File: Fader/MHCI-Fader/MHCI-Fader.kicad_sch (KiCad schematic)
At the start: 1 part

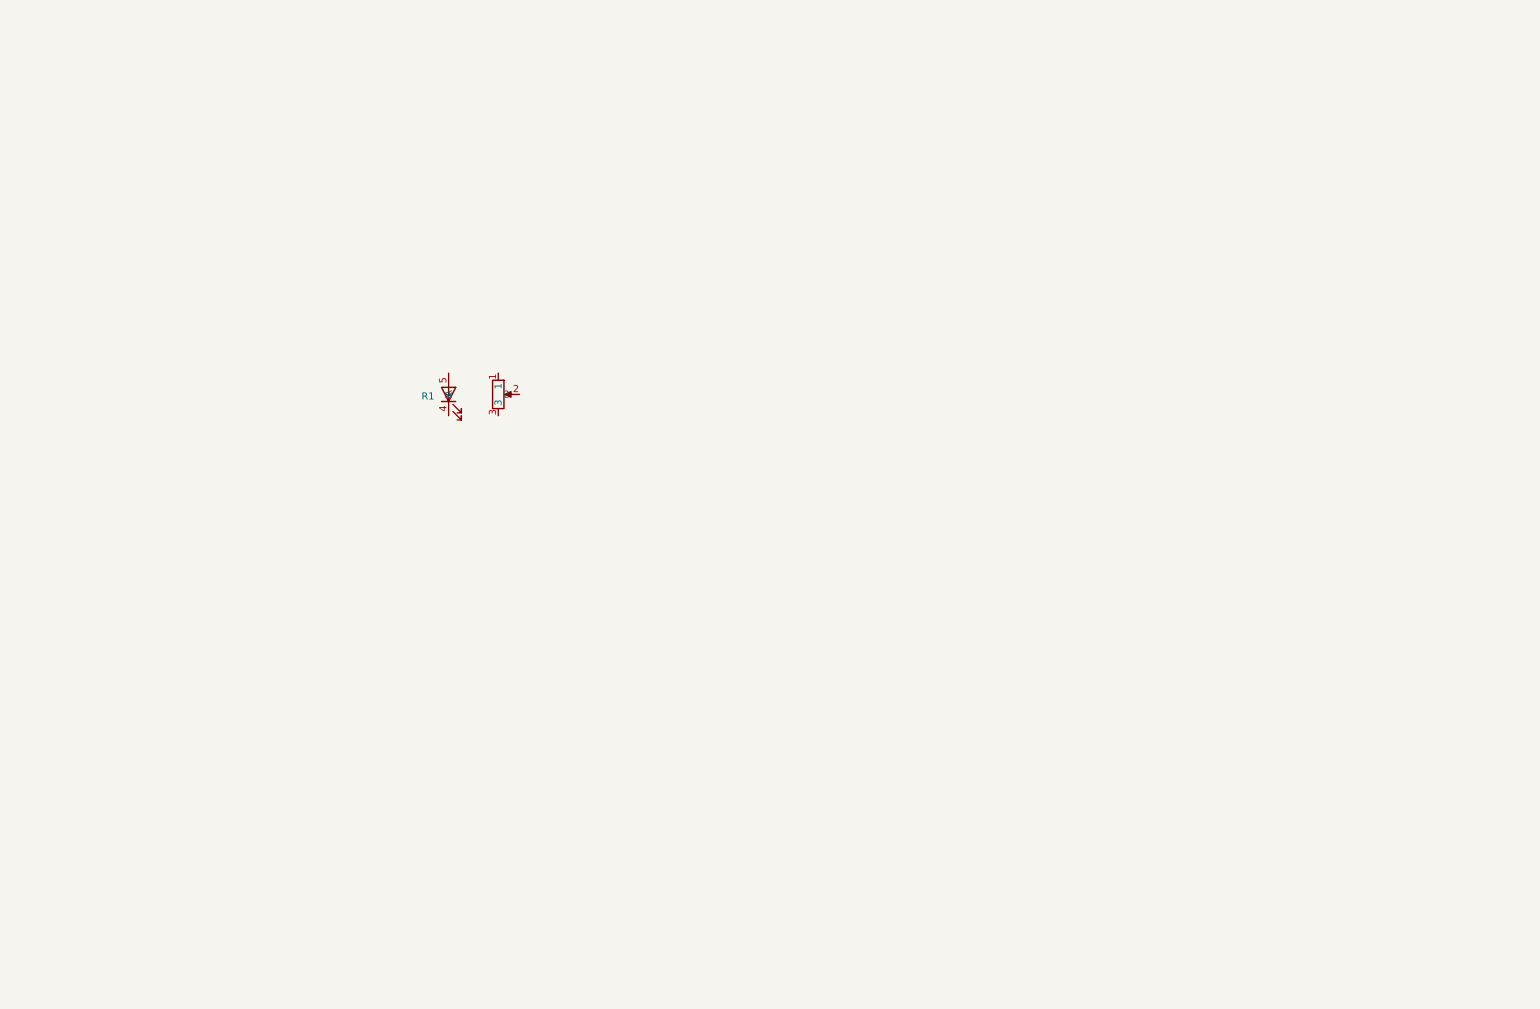
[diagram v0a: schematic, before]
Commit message: Add all Waveshare footprints
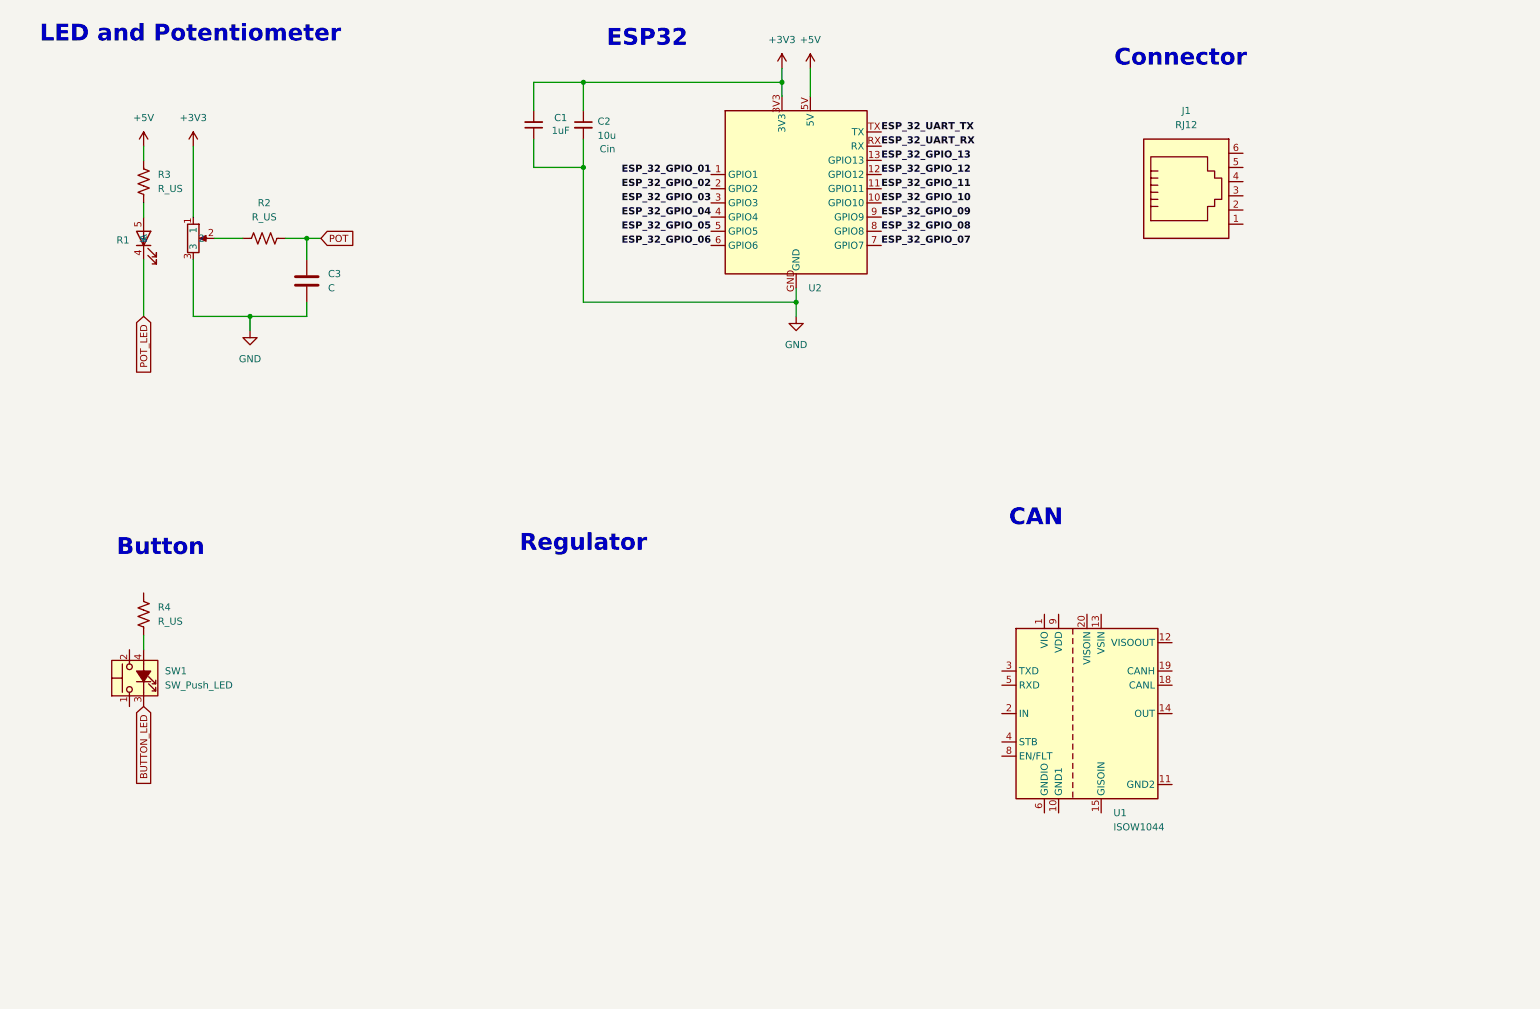
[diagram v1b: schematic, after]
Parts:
- added C1: 1uF, Capacitor_SMD:C_0402_1005Metric, symbol Device:C_Small
- added C2: 10u, Capacitor_SMD:C_0603_1608Metric, symbol Device:C_Small
- added C3: C, symbol Device:C
- added J1: RJ12, Connector_RJ:RJ12_Amphenol_54601-x06_Horizontal, symbol Connector:RJ12
- added R2, R3, R4: R_US, symbol Device:R_US
- added SW1: SW_Push_LED, MCHI:SP86N_AB Switch, symbol Switch:SW_Push_LED
- added U1: ISOW1044, Package_SO:SOIC-20W_7.5x12.8mm_P1.27mm, symbol Interface_CAN_LIN:ISOW1044
- added U2: ~, MCHI:ESP-32-S3-Zero - SMD, symbol MHCI:ESP32-S3-Zero
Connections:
- net +3V3: now reaches R1.1
- net +3V3: now also C1.2, C2.1, U2.3V3
- net at R1.2: now also R2.1
- net GND: now reaches R1.3
- net GND: now also C1.1, C2.2, C3.2, U2.GND
- net POT_LED: now reaches R1.4 (K)
- net at R1.5 (A): now also R3.1
- new net: U1.15 (GISOIN), U1.16 (GISOIN), U1.17 (GISOIN)
- new net: R4.1, SW1.4 (A)
- new net +5V: R3.2, U2.5V
- new net BUTTON_LED: SW1.3 (K)
- new net ESP_32_GPIO_01: U2.1 (GPIO1)
- new net ESP_32_GPIO_02: U2.2 (GPIO2)
- new net ESP_32_GPIO_03: U2.3 (GPIO3)
- new net ESP_32_GPIO_04: U2.4 (GPIO4)
- new net ESP_32_GPIO_05: U2.5 (GPIO5)
- new net ESP_32_GPIO_06: U2.6 (GPIO6)
- new net ESP_32_GPIO_07: U2.7 (GPIO7)
- new net ESP_32_GPIO_08: U2.8 (GPIO8)
- new net ESP_32_GPIO_09: U2.9 (GPIO9)
- new net ESP_32_GPIO_10: U2.10 (GPIO10)
- new net ESP_32_GPIO_11: U2.11 (GPIO11)
- new net ESP_32_GPIO_12: U2.12 (GPIO12)
- new net ESP_32_GPIO_13: U2.13 (GPIO13)
- new net ESP_32_UART_RX: U2.RX
- new net ESP_32_UART_TX: U2.TX
- new net POT: C3.1, R2.2
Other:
- note added: "Button"
- note added: "CAN"
- note added: "Connector"
- note added: "ESP32"
- note added: "LED and Potentiometer"
- note added: "Regulator"
- moved on the sheet: R1

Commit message: Initial fader schematic
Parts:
- removed C3: C, symbol Device:C
- removed J1: RJ12, Connector_RJ:RJ12_Amphenol_54601-x06_Horizontal, symbol Connector:RJ12
- removed U1: ISOW1044, Package_SO:SOIC-20W_7.5x12.8mm_P1.27mm, symbol Interface_CAN_LIN:ISOW1044
- added C3: 10uF, Capacitor_SMD:C_0603_1608Metric, symbol Device:C_Small
- added C4: 1uF, Capacitor_SMD:C_0402_1005Metric, symbol Device:C_Small
- added C5, C7: 100nF, Capacitor_SMD:C_0402_1005Metric, symbol Device:C_Small
- added C6: 1u, Capacitor_SMD:C_0402_1005Metric, symbol Device:C_Small
- added C8: 30pF, Capacitor_SMD:C_0402_1005Metric, symbol Device:C_Small
- added FB1: FerriteBead, Diode_SMD:D_0805_2012Metric, symbol Device:FerriteBead_Small
- added J1: Conn_01x06, Connector_PinHeader_2.54mm:PinHeader_1x06_P2.54mm_Vertical, symbol Connector_Generic:Conn_01x06
- added JP1, JP2: Jumper_2_Open, Jumper:SolderJumper-2_P1.3mm_Open_RoundedPad1.0x1.5mm, symbol Jumper:Jumper_2_Open
- added PS1: TBA1-0510, MCHI:CONV_TBA1-0510, symbol MHCI:TBA1-0510
- added R10, R9: 0R, Resistor_SMD:R_0402_1005Metric, symbol Device:R_US
- added R5, R6: 4K7, Resistor_SMD:R_0603_1608Metric, symbol Device:R_US
- added R7: 10K, Resistor_SMD:R_0402_1005Metric, symbol Device:R_US
- added R8: 120R, Resistor_SMD:R_0402_1005Metric, symbol Device:R_US
- added TP1: VIN, TestPoint:TestPoint_Pad_D1.0mm, symbol Connector:TestPoint
- added TP2: 5V, TestPoint:TestPoint_Pad_D1.0mm, symbol Connector:TestPoint
- added U1: TJA1051T, Package_SO:SOIC-8_3.9x4.9mm_P1.27mm, symbol Interface_CAN_LIN:TJA1051T
- added U3: SRV05-4, Package_TO_SOT_SMD:SOT-23-6, symbol Power_Protection:SRV05-4
- C1: value 1uF -> 100nF; LCSC C52923 -> C1525
- C2: value 10u -> 30pF; footprint Capacitor_SMD:C_0603_1608Metric -> Capacitor_SMD:C_0402_1005Metric; LCSC C19702 -> C1570
- R2, R3, R4: value R_US -> 220R; footprint (none) -> Resistor_SMD:R_0402_1005Metric; LCSC (none) -> C25091
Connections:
- net +3V3: now also R3.2, R4.2, PS1.4 (+VOUT), R5.1, R6.1, R7.1; no longer C1.2, C2.1
- net +5V: now also C1.1, C5.1, FB1.2, JP1.2 (B), PS1.2 (+VIN(VCC)), TP2.1, U1.3 (VCC); no longer R3.2, U2.5V
- net BUTTON_LED: now also C6.1, R7.2
- net GND: now also C1.2, C2.1, SW1.1, C6.2, C7.2, C8.2, PS1.3 (-VOUT), U1.2 (GND); no longer C1.1, C2.2
- net POT: now also R2.1, C7.1; no longer R2.2
- net at R1.2: now also R2.2; no longer R2.1
- new net: JP2.1 (A), R8.2
- new net: JP1.1 (A), U2.5V
- new net CANH: C8.1, J1.4 (Pin_4), R9.1, U3.4 (IO3)
- new net CANH_L: JP2.2 (B), R10.1, U1.6 (CANL)
- new net CANH_T: R8.1, R9.2, U1.7 (CANH)
- new net CANL: C2.2, J1.5 (Pin_5), R10.2, U3.6 (IO4)
- new net CAN_RX: U1.4 (RXD)
- new net CAN_S: U1.8 (S)
- new net CAN_TX: U1.1 (TXD)
- new net Earth: C3.2, C4.1, C5.2, J1.6 (Pin_6), PS1.1 (-VIN(GND)), U3.2 (VN)
- new net SCL: J1.3 (Pin_3), R6.2, U3.3 (IO2)
- new net SDA: J1.2 (Pin_2), R5.2, U3.1 (IO1)
- new net VIN: C3.1, C4.2, FB1.1, J1.1 (Pin_1), TP1.1, U3.5 (VP)
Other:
- note added: "I2C"
- note added: "Power Regulator"
- note added: "Termination"
- note removed: "Regulator"
- moved on the sheet: R1, R3, SW1, U2

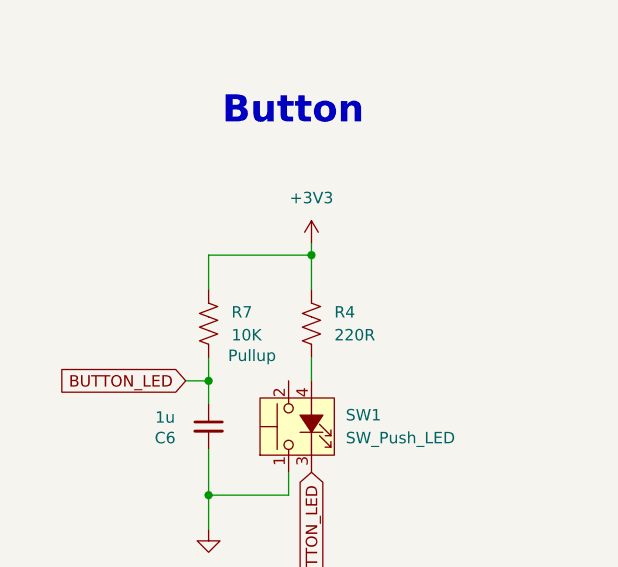
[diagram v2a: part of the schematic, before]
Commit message: Fix button schematic
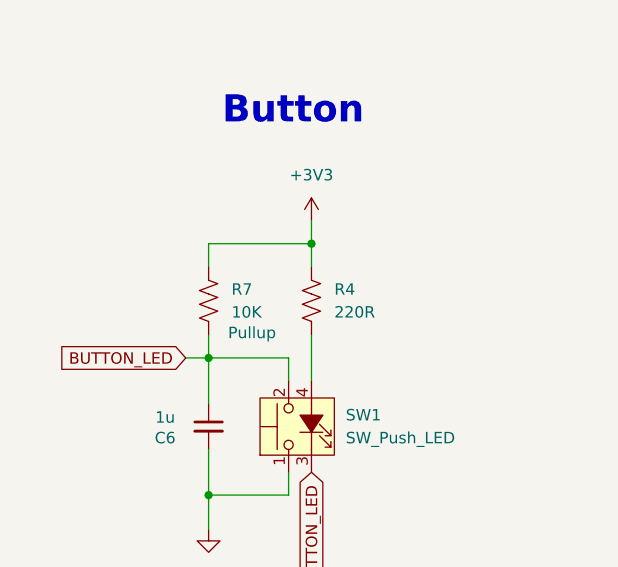
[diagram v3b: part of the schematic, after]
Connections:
- net BUTTON_LED: now also SW1.2
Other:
- moved on the sheet: R4, R7
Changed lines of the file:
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@@
 	(paper "A4")
 	(junction
-		(at 36.83 116.84)
-		(diameter 0)
-		(color 0 0 0 0)
-	)
-	(junction
 		(at 53.34 170.18)
 		(diameter 0)
@@
 	)
 	(junction
-		(at 68.58 170.18)
+		(at 48.26 101.6)
 		(diameter 0)
 		(color 0 0 0 0)
 	)
 	(junction
-		(at 222.25 102.87)
+		(at 68.58 170.18)
 		(diameter 0)
 		(color 0 0 0 0)
 	)
 	(junction
-		(at 48.26 102.87)
+		(at 222.25 102.87)
 		(diameter 0)
 		(color 0 0 0 0)
@@
 	)
 	(junction
+		(at 36.83 114.3)
+		(diameter 0)
+		(color 0 0 0 0)
+	)
+	(junction
 		(at 53.34 181.61)
 		(diameter 0)
@@
 	(wire
 		(pts
-			(xy 262.89 130.81) (xy 262.89 133.35)
+			(xy 45.72 114.3) (xy 45.72 116.84)
 		)
 		(stroke
@@
 	(wire
 		(pts
-			(xy 36.83 116.84) (xy 36.83 119.38)
+			(xy 262.89 130.81) (xy 262.89 133.35)
 		)
 		(stroke
@@
 	(wire
 		(pts
-			(xy 48.26 102.87) (xy 48.26 106.68)
-		)
-		(stroke
-			(width 0)
-			(type default)
-		)
-	)
-	(wire
-		(pts
 			(xy 252.73 130.81) (xy 252.73 128.27)
 		)
@@
 	(wire
 		(pts
-			(xy 36.83 114.3) (xy 36.83 116.84)
-		)
-		(stroke
-			(width 0)
-			(type default)
-		)
-	)
-	(wire
-		(pts
 			(xy 43.18 63.5) (xy 53.34 63.5)
 		)
@@
 	(wire
 		(pts
-			(xy 34.29 116.84) (xy 36.83 116.84)
+			(xy 34.29 114.3) (xy 36.83 114.3)
 		)
 		(stroke
@@
 	(wire
 		(pts
-			(xy 48.26 102.87) (xy 48.26 101.6)
-		)
-		(stroke
-			(width 0)
-			(type default)
-		)
-	)
-	(wire
-		(pts
 			(xy 43.18 33.02) (xy 43.18 45.72)
 		)
@@
 	(wire
 		(pts
+			(xy 48.26 99.06) (xy 48.26 101.6)
+		)
+		(stroke
+			(width 0)
+			(type default)
+		)
+	)
+	(wire
+		(pts
 			(xy 33.02 163.83) (xy 33.02 170.18)
 		)
@@
 	(wire
 		(pts
+			(xy 36.83 114.3) (xy 36.83 119.38)
+		)
+		(stroke
+			(width 0)
+			(type default)
+		)
+	)
+	(wire
+		(pts
 			(xy 36.83 129.54) (xy 36.83 133.35)
 		)
@@
 	(wire
 		(pts
+			(xy 48.26 101.6) (xy 48.26 104.14)
+		)
+		(stroke
+			(width 0)
+			(type default)
+		)
+	)
+	(wire
+		(pts
+			(xy 36.83 114.3) (xy 45.72 114.3)
+		)
+		(stroke
+			(width 0)
+			(type default)
+		)
+	)
+	(wire
+		(pts
 			(xy 53.34 66.04) (xy 53.34 63.5)
 		)
@@
 	(wire
 		(pts
+			(xy 36.83 111.76) (xy 36.83 114.3)
+		)
+		(stroke
+			(width 0)
+			(type default)
+		)
+	)
+	(wire
+		(pts
 			(xy 219.71 44.45) (xy 219.71 46.99)
 		)
@@
 	(wire
 		(pts
-			(xy 36.83 102.87) (xy 48.26 102.87)
+			(xy 36.83 101.6) (xy 48.26 101.6)
 		)
 		(stroke
@@
 	(wire
 		(pts
-			(xy 48.26 114.3) (xy 48.26 116.84)
+			(xy 48.26 111.76) (xy 48.26 116.84)
 		)
 		(stroke
@@
 	(wire
 		(pts
-			(xy 36.83 106.68) (xy 36.83 102.87)
+			(xy 36.83 104.14) (xy 36.83 101.6)
 		)
 		(stroke
@@
 	(global_label "BUTTON_LED"
 		(shape input)
-		(at 34.29 116.84 180)
+		(at 34.29 114.3 180)
 		(fields_autoplaced yes)
 		(effects
@@
 		)
 		(property "Intersheetrefs" "${INTERSHEET_REFS}"
-			(at 19.6934 116.84 0)
+			(at 19.6934 114.3 0)
 			(effects
 				(font
@@
 	(symbol
 		(lib_id "Device:R_US")
-		(at 48.26 110.49 180)
+		(at 48.26 107.95 180)
 		(unit 1)
 		(exclude_from_sim no)
@@
 		(fields_autoplaced yes)
 		(property "Reference" "R4"
-			(at 50.8 109.2199 0)
+			(at 50.8 106.6799 0)
 			(effects
 				(font
@@
 		)
 		(property "Value" "220R"
-			(at 50.8 111.7599 0)
+			(at 50.8 109.2199 0)
 			(effects
 				(font
@@
 		)
 		(property "Footprint" "Resistor_SMD:R_0402_1005Metric"
-			(at 47.244 110.236 90)
+			(at 47.244 107.696 90)
 			(effects
 				(font
@@
 		)
 		(property "Datasheet" "~"
-			(at 48.26 110.49 0)
+			(at 48.26 107.95 0)
 			(effects
 				(font
@@
 		)
 		(property "Description" "Resistor, US symbol"
-			(at 48.26 110.49 0)
+			(at 48.26 107.95 0)
 			(effects
 				(font
@@
 		)
 		(property "LCSC" "C25091"
-			(at 48.26 110.49 0)
+			(at 48.26 107.95 0)
 			(effects
 				(font
@@
 	(symbol
 		(lib_id "power:+3V3")
-		(at 48.26 101.6 0)
+		(at 48.26 99.06 0)
 		(unit 1)
 		(exclude_from_sim no)
@@
 		(fields_autoplaced yes)
 		(property "Reference" "#PWR013"
-			(at 48.26 105.41 0)
+			(at 48.26 102.87 0)
 			(effects
 				(font
@@
 		)
 		(property "Value" "+3V3"
-			(at 48.26 96.52 0)
+			(at 48.26 93.98 0)
 			(effects
 				(font
@@
 		)
 		(property "Footprint" ""
-			(at 48.26 101.6 0)
+			(at 48.26 99.06 0)
 			(effects
 				(font
@@
 		)
 		(property "Datasheet" ""
-			(at 48.26 101.6 0)
+			(at 48.26 99.06 0)
 			(effects
 				(font
@@
 		)
 		(property "Description" "Power symbol creates a global label with name \"+3V3\""
-			(at 48.26 101.6 0)
+			(at 48.26 99.06 0)
 			(effects
 				(font
@@
 	(symbol
 		(lib_id "Device:R_US")
-		(at 36.83 110.49 0)
+		(at 36.83 107.95 0)
 		(unit 1)
 		(exclude_from_sim no)
@@
 		(dnp no)
 		(property "Reference" "R7"
-			(at 39.37 109.2199 0)
+			(at 39.37 106.6799 0)
 			(effects
 				(font
@@
 		)
 		(property "Value" "10K"
-			(at 39.37 111.7599 0)
+			(at 39.37 109.2199 0)
 			(effects
 				(font
@@
 		)
 		(property "Footprint" "Resistor_SMD:R_0402_1005Metric"
-			(at 37.846 110.744 90)
+			(at 37.846 108.204 90)
 			(effects
 				(font
@@
 		)
 		(property "Datasheet" "~"
-			(at 36.83 110.49 0)
+			(at 36.83 107.95 0)
 			(effects
 				(font
@@
 		)
 		(property "Description" "Pullup"
-			(at 41.656 114.046 0)
+			(at 41.656 111.506 0)
 			(effects
 				(font
@@
 		)
 		(property "LCSC" "C25744"
-			(at 36.83 110.49 0)
+			(at 36.83 107.95 0)
 			(effects
 				(font
